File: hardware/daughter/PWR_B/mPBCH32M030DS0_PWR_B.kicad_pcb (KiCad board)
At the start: 2 copper layers, 43.2 x 66.9 mm, 73 parts, among them J1 SOCK_L, J2 SOCK_R, J3 PWR_IN, J4 MOTOR, Q1 TKR74F04PB, Q10 TPN1R603PL, Q2 TKR74F04PB, Q3 TKR74F04PB, Q4 TKR74F04PB, Q5 TKR74F04PB, Q6 TKR74F04PB, Q7 TKR74F04PB, Q8 TKR74F04PB, Q9 TPN2R304PL, U2 78L05, U4 LM74700-Q1, U5 LM74700-Q1

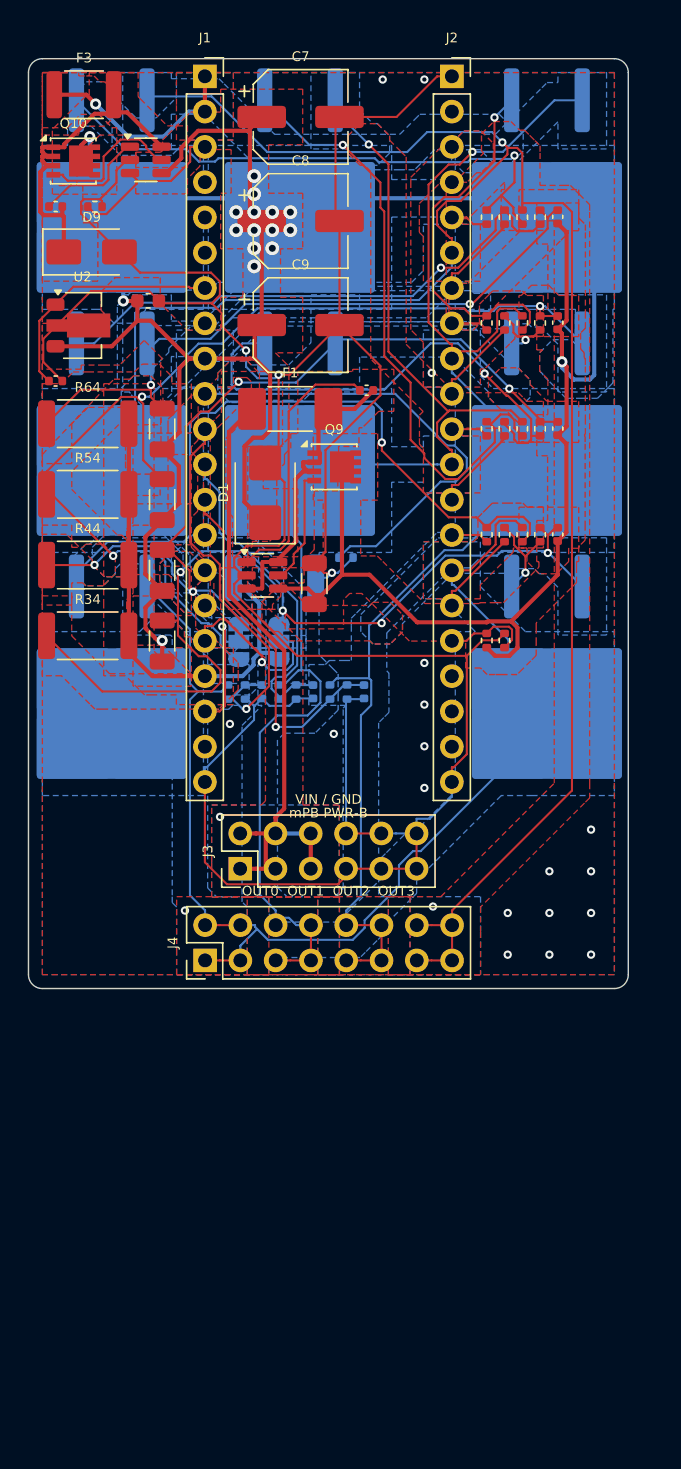
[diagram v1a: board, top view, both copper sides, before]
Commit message: 子基板 B を 44.6 x 99.5mm に拡大: M3 丸端子台 x6・ヒートシンク固定穴 x2・電源ベタのはんだ盛り
- 電源 (J3 VIN / J5 GND) と 4 相出力 (J40〜J43) を Würth REDCUBE の M3 丸端子台で受ける
- ヒートシンク固定用 M3 穴 H1/H2。MOSFET・シャントは BOTTOM 面 (ヒートシンク側) に 4 レッグ横並び
- 大電流の銅箔を配線前に固定ベタとして置き, レジスト開口ではんだを盛れるようにした
- 右端の VBUS 帯を表裏 2 層に, レッグ 3 横のネックを裏で迂回, 上端に USB 帰路の GND 帯
- 電流容量 (1 相): 1oz 5.4A / はんだ 0.3mm 7.4A。USB-PD 経路は 3A まで
- D1/C1 の − 側は ISH。面付けパネル (99.94 x 99.76mm), 製造データ, 資料を更新

Co-Authored-By: Claude Opus 5.5 <noreply@anthropic.com>
Claude-Session: https://claude.ai/code/session_01LENFjjhDfYjJZV1NWhB9uV
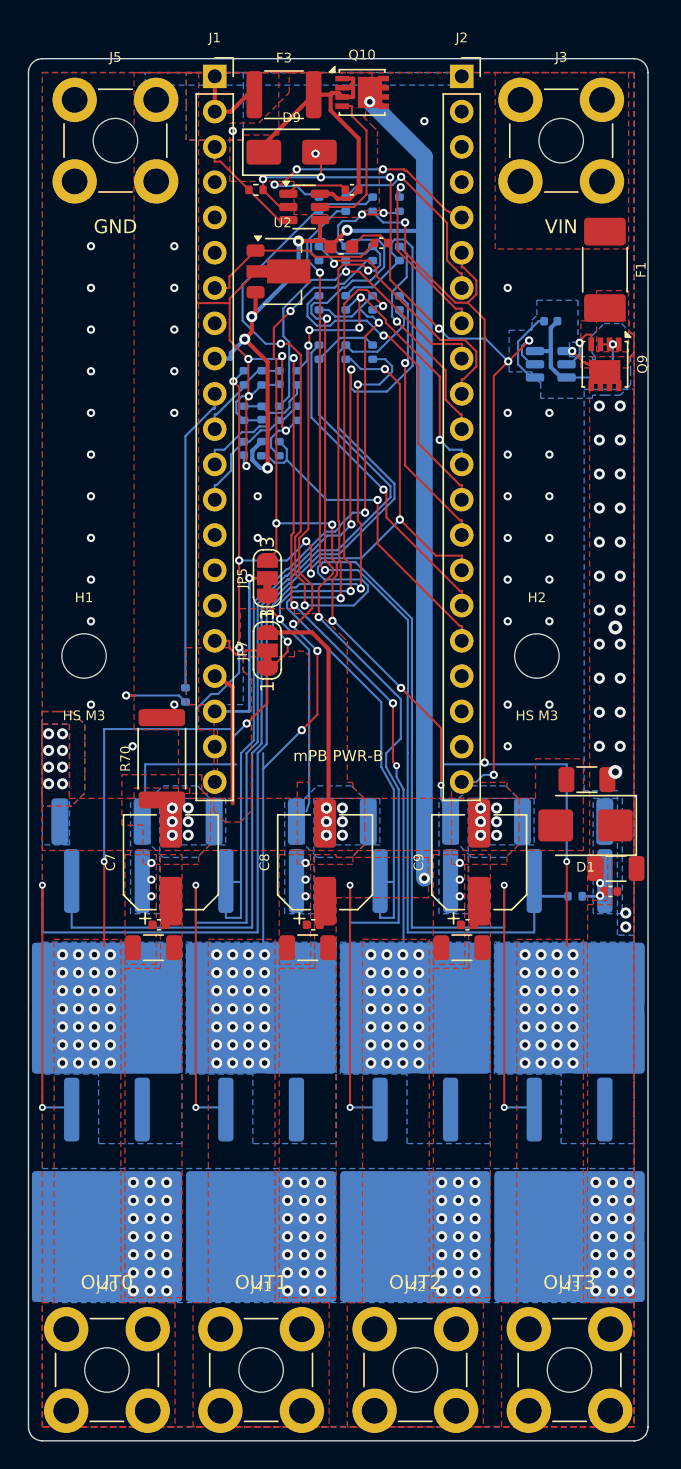
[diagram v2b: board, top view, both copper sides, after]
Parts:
- removed J4: MOTOR, PinHeader_2x08_P2.54mm_Vertical
- added H1: HEATSINK_M3, MountingHole_3.2mm_M3, F.Cu at (4.00, 43.0)
- added H2: HEATSINK_M3, MountingHole_3.2mm_M3, F.Cu at (36.6, 43.0)
- added J40: OUT0, Wuerth_REDCUBE-THR_WP-THRBU_74650073_THR, F.Cu at (5.65, 94.4)
- added J41: OUT1, Wuerth_REDCUBE-THR_WP-THRBU_74650073_THR, F.Cu at (16.8, 94.4)
- added J42: OUT2, Wuerth_REDCUBE-THR_WP-THRBU_74650073_THR, F.Cu at (27.9, 94.4)
- added J43: OUT3, Wuerth_REDCUBE-THR_WP-THRBU_74650073_THR, F.Cu at (38.9, 94.4)
- added J5: GND, Wuerth_REDCUBE-THR_WP-THRBU_74650073_THR, F.Cu at (6.26, 5.90)
- C5, R11, R12, R30, R31, R32, R33, R34, R40, R41, R42, R43, R44, R50, R51, R52, R53, R54, R60, R61, R62, R63, R64, U4: moved to B.Cu
- J3: value PWR_IN -> VIN; footprint PinHeader_2x06_P2.54mm_Vertical -> Wuerth_REDCUBE-THR_WP-THRBU_74650073_THR
- JP5, JP7, R70: moved to F.Cu
- moved Q7 79.8 mm to (38.9, 83.3)
- moved Q5 73.3 mm to (27.9, 83.3)
- moved Q3 72.7 mm to (16.8, 83.3)
- moved J3 57.3 mm to (38.4, 5.90), turned to 0 degrees
- moved C7 54.5 mm to (10.2, 57.9), turned to 90 degrees
- moved Q8 50.8 mm to (38.9, 66.8)
- moved R63 49.0 mm to (39.4, 60.3), turned to 0 degrees
- moved C60 48.7 mm to (41.9, 60.0), turned to 180 degrees
- moved C8 46.2 mm to (21.4, 57.9), turned to 90 degrees
- moved C61 45.5 mm to (42.3, 58.3), turned to 180 degrees
- moved R64 44.7 mm to (38.5, 54.9), turned to 180 degrees
- moved C50 43.8 mm to (31.6, 62.4), turned to 180 degrees
- moved C9 40.8 mm to (32.5, 57.9), turned to 90 degrees
- moved C30 40.2 mm to (9.40, 62.4), turned to 180 degrees
- moved Q6 39.8 mm to (27.9, 66.8)
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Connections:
- C1 pad 2: GND -> ISH
- C7 pad 2: GND -> ISH
- C8 pad 2: GND -> ISH
- C9 pad 2: GND -> ISH
- D1 pad 2: GND -> ISH
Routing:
- net VBUS: track 253.3 -> 97.6 mm, vias 17 -> 118
- net GND: track 213.3 -> 115.4 mm, vias 20 -> 51
- net SW3: track 160.3 -> 71.0 mm, vias 2 -> 31
- net GH3: track 41.2 -> 106.9 mm, vias 1 -> 4
- net GH2: track 26.5 -> 91.3 mm, vias 1 -> 6
- net GL2: track 5.04 -> 67.9 mm, vias 1 -> 2
- net GL0: track 6.77 -> 69.1 mm, vias 1 -> 0
- net GH1: track 44.0 -> 91.8 mm, vias 1 -> 4
- net SRC3: track 48.3 -> 1.04 mm
- net VIN: track 45.9 -> 0.00 mm, vias 1 -> 0
- net GH0: track 51.0 -> 92.8 mm, vias 1 -> 2
- net GL3: track 39.0 -> 73.1 mm, vias 1 -> 2
- net SW2: track 102.7 -> 71.8 mm, vias 2 -> 33
- net SW1: track 104.9 -> 74.7 mm, vias 1 -> 36
- net SRC2: track 75.7 -> 53.9 mm, vias 3 -> 9
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- added copper zone on B.Cu, net VIN_F
- removed copper zone on B.Cu, net VIN
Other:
- board size 43.2 x 66.9 mm -> 44.6 x 99.5 mm
- board text added: "GND"
- board text added: "HS M3"
- board text added: "OUT0"
- board text added: "OUT1"
- board text added: "OUT2"
- board text added: "OUT3"
- board text added: "VIN"
- board text removed: "OUT0 OUT1 OUT2 OUT3"
- board text removed: "VIN / GND"
